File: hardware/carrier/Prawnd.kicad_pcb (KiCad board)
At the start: 2 copper layers, 100 x 60 mm, 19 parts, among them J1 ESP32 L, J2 ESP32 R, J3 Mic1 R, J4 Mic1 L, J5 Mic2 R, J6 Mic2 L, J7 SD Card, J8 BTN

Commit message: hardware: carrier rev 2 — J7 reordered for mini 3.3V SD module; bench-test firmware
Rev 1's J7 used the HW-125-style order (GND VCC MISO MOSI SCK CS), but
HW-125 modules are 5V boards (AMS1117 + level shifter) and brown out on
the carrier's 3.3V rail — the card never answers GO_IDLE. Rev 2 targets
the regulator-less mini 3.3V module instead:

- J7 reordered to GND MISO CLK MOSI CS 3V3 (pin 1→6), silk updated
- SD_SCK/SD_MISO swapped onto GPIO20/GPIO19 via the C6 GPIO matrix so
  all three SPI lines route as parallel B.Cu diagonals — no crossings,
  no vias; pins.h updated to match (rev 1 SD wiring no longer matches
  firmware — swap the two wires or revert pins.h to bench SD on rev 1)
- DRC: 0 errors / 0 unconnected to OSH Park 2-layer rules; two rev-1
  hole_clearance warnings gone; fit-check PDF regenerated
- wiring.md: BOM names the mini 3.3V module + HW-125 warning, pin map
  and diagrams updated for the SCK/MISO swap, rev 1 vs rev 2 note

Also adds bench bring-up envs used to validate rev 1 (LED + both mics
PASS, SD blocked on the 5V module): src/bringup/ with mictest (mic
level meter + LED), blinktest (D1 LED only), boardtest (LED + SD
write/read-back + 10s WAV record + live meter).

Co-Authored-By: Claude Fable 5 <noreply@anthropic.com>
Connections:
- J2 pad 5: SD_MISO -> SD_SCK
- J2 pad 6: SD_SCK -> SD_MISO
- J7 pad 2: +3V3 -> SD_MISO
- J7 pad 3: SD_MISO -> SD_SCK
- J7 pad 5: SD_SCK -> SD_CS
- J7 pad 6: SD_CS -> +3V3
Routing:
- net SD_CS: track 26.7 -> 39.5 mm
- net +3V3: track 199.4 -> 203.0 mm
- net SD_MISO: track 46.3 -> 42.8 mm
- net SD_SCK: track 39.7 -> 42.8 mm
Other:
- board text removed: "VCC"

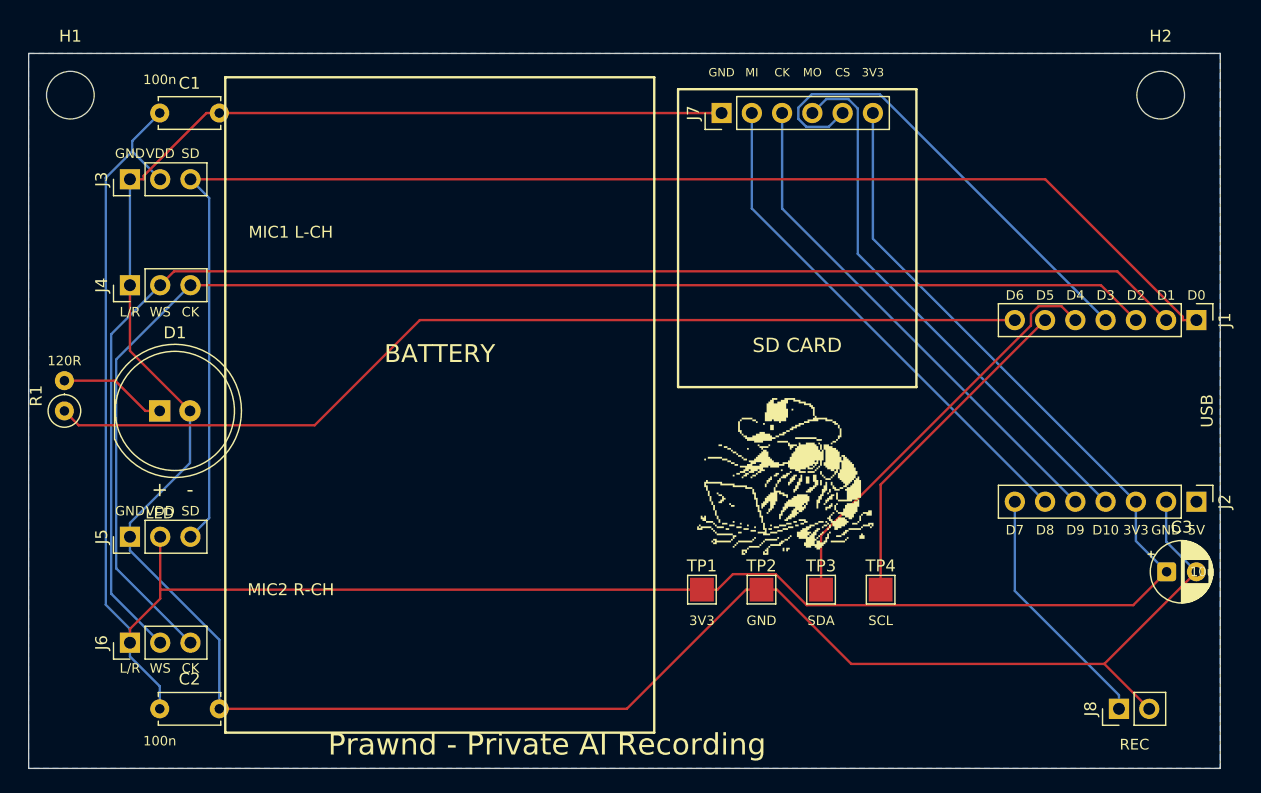
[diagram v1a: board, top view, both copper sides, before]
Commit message: hardware: fix illegible silk labels, stamp rev 2
Rev 1 fab exposed several silk collisions that printed as mush or not at
all: C3's refdes sat on J2's 5V/GND pin labels (the mystery unlabeled
half-shaded circle), the 10u value text crossed C3's own polarity arc and
GND pad, C2's refdes landed on the mic CK pin label, the LED text printed
on top of a VDD pin label, and J1/J2's refdes were past the board edge.

- Relocate C3/C2/J1/J2 refdes and the 10u text to clear ground
- Move LED inside the D1 circle (visible until the LED is fitted)
- Bump J7 pin labels 0.7 -> 0.8mm tall (0.6mm wide, still fits the pitch)
- Add 'rev 2' stamp next to the title text
- DRC silk warnings 29 -> 7; the rest are the intentional bay outlines
  crossing parts and the D1 lib-mismatch note. Fit-check PDF regenerated.

Co-Authored-By: Claude Fable 5 <noreply@anthropic.com>
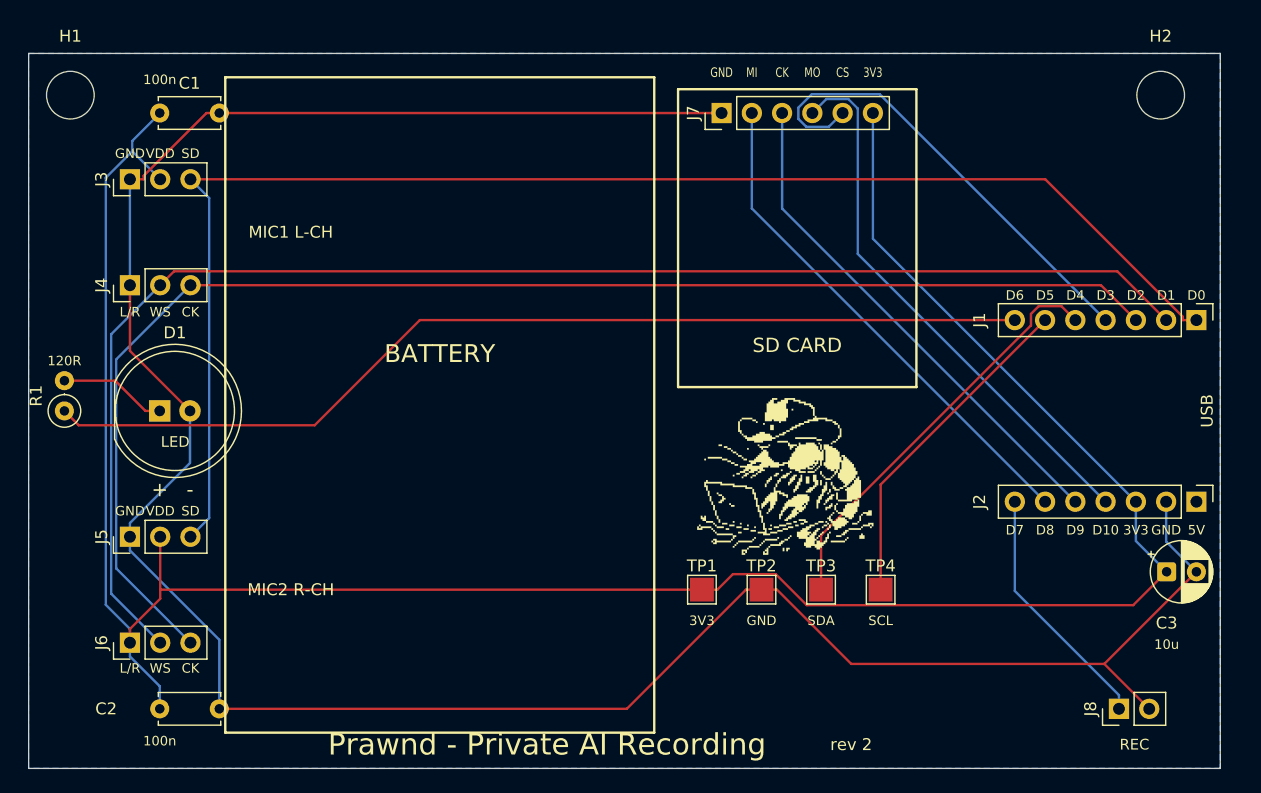
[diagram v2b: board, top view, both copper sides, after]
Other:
- board text added: "rev 2"
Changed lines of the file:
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@@
 		(tags "Through hole pin header THT 1x07 2.54mm single row")
 		(property "Reference" "J2"
-			(at 0 -2.38 270)
+			(at 0 18.2 270)
 			(layer "F.SilkS")
 			(effects
@@
 		(tags "CP Radial series Radial pin pitch 2.50mm diameter 5mm height 7mm Electrolytic Capacitor")
 		(property "Reference" "C3"
-			(at 1.25 -3.75 0)
+			(at 0 4.3 0)
 			(layer "F.SilkS")
 			(effects
@@
 		)
 		(property "Value" "10u"
-			(at 1.25 3.75 0)
+			(at 0 6.1 0)
 			(layer "F.Fab")
 			(effects
@@
 		(tags "C Disc series Radial pin pitch 5.00mm diameter 5mm width 2.5mm Capacitor")
 		(property "Reference" "C2"
-			(at 2.5 -2.5 0)
+			(at -4.5 0 0)
 			(layer "F.SilkS")
 			(effects
@@
 		(tags "Through hole pin header THT 1x07 2.54mm single row")
 		(property "Reference" "J1"
-			(at 0 -2.38 270)
+			(at 0 18.2 270)
 			(layer "F.SilkS")
 			(effects
@@
 		(effects
 			(font
-				(size 0.7 0.7)
+				(size 0.8 0.6)
 				(thickness 0.13)
 			)
@@
 		(effects
 			(font
-				(size 0.7 0.7)
+				(size 0.8 0.6)
 				(thickness 0.13)
 			)
@@
 		(effects
 			(font
-				(size 0.7 0.7)
+				(size 0.8 0.6)
 				(thickness 0.13)
 			)
@@
 		(effects
 			(font
-				(size 0.7 0.7)
+				(size 0.8 0.6)
 				(thickness 0.13)
 			)
@@
 		(effects
 			(font
-				(size 0.7 0.7)
+				(size 0.8 0.6)
 				(thickness 0.13)
 			)
@@
 		(effects
 			(font
-				(size 0.7 0.7)
+				(size 0.8 0.6)
 				(thickness 0.13)
 			)
@@
 		)
 	)
-	(gr_text "D0"
-		(at 249.5 81.3 0)
+	(gr_text "10u"
+		(at 247 110.6 0)
 		(layer "F.SilkS")
 		(effects
@@
 		)
 	)
-	(gr_text "5V"
-		(at 249.5 101 0)
+	(gr_text "D0"
+		(at 249.5 81.3 0)
 		(layer "F.SilkS")
 		(effects
@@
 		)
 	)
-	(gr_text "10u"
-		(at 250 104.5 0)
+	(gr_text "5V"
+		(at 249.5 101 0)
 		(layer "F.SilkS")
 		(effects
@@
 	)
 	(gr_text "LED"
-		(at 162.5 99.6 0)
+		(at 163.8 93.6 0)
 		(layer "F.SilkS")
 		(effects
@@
 		(layer "F.SilkS")
 		(effects
+			(font
+				(size 1 1)
+				(thickness 0.15)
+			)
+		)
+	)
+	(gr_text "rev 2"
+		(at 220.527142 119 0)
+		(layer "F.SilkS")
+		(effects
